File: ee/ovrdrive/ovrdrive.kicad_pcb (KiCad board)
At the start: 4 copper layers, 36.4 x 15 mm, 53 parts, among them J2 USB3_A, J4 Micro_SD_Card_Det_Hirose_DM3AT, SW1 SW_Push, U1 CH569W, U2 TLV62569DBV, U3 TLV62569DBV, Y2 30Mhz

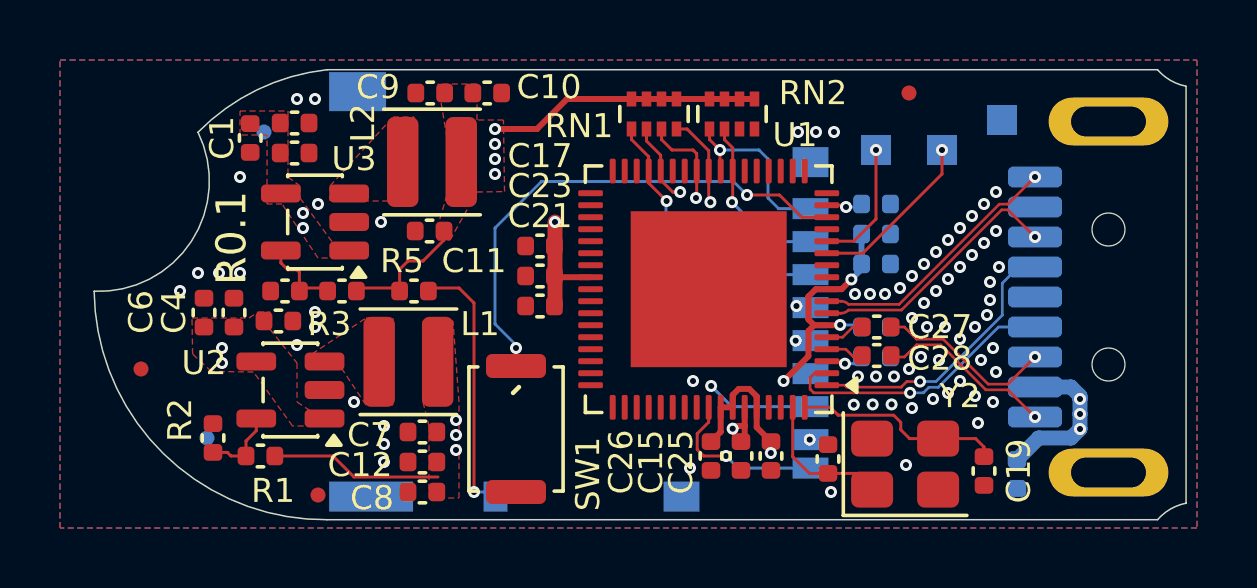
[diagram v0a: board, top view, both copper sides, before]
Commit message: Fixed SDIO pinout, length matched SDIO traces.
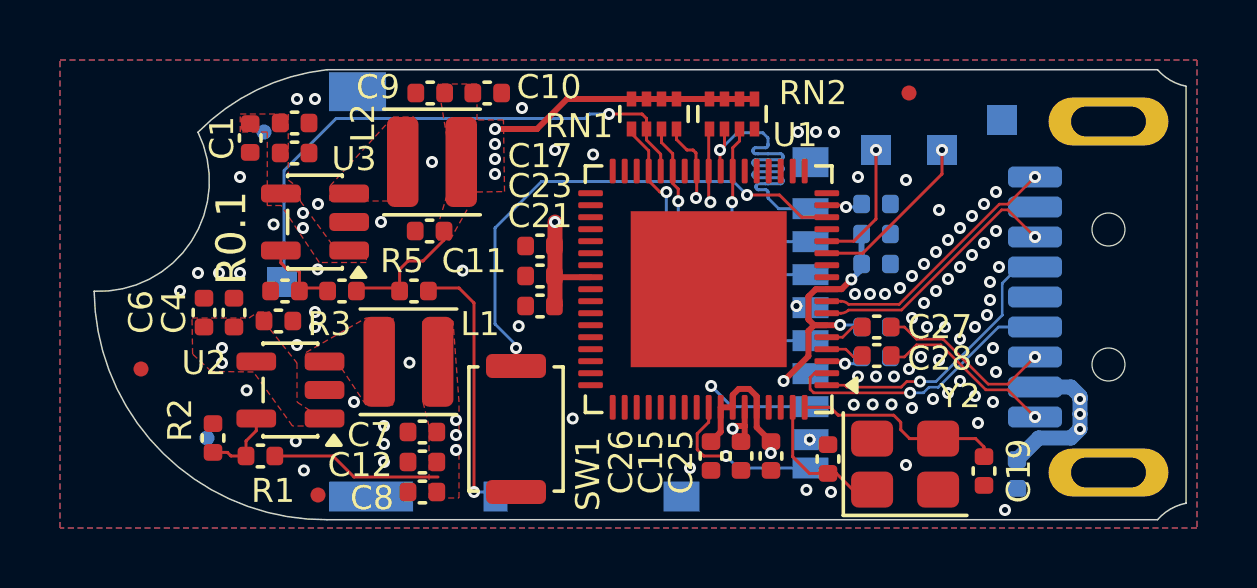
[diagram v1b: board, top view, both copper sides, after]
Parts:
- added TP4: TestPoint, TestPoint:TestPoint_Pad_1.0x1.0mm, B.Cu at (114.3, 103.7)
- C19, C20: value ? -> 15pF
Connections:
- RN1 pad 1: /SD_CMD -> /SD_CLK
- RN1 pad 2: /SD_CLK -> /RST#
- RN1 pad 3: /SD_D0 -> /SD_CMD
- RN1 pad 4: /SD_D1 -> /SD_D0
- RN2 pad 1: /SD_D2 -> /SD_D1
- RN2 pad 2: /SD_D3 -> /SD_D2
- RN2 pad 3: unconnected-(RN2-R3.1-Pad3) -> /SD_D3
- U1 pad 29: unconnected-(U1-PB16-Pad29) -> /SD_CMD
- U1 pad 30: /SD_CLK -> /RST#
- U1 pad 31: /SD_CMD -> /SD_CLK
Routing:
- net /RST#: track 0.00 -> 18.6 mm, vias 0 -> 1
- net /SD_D3: track 5.73 -> 12.7 mm
- net /SD_D2: track 6.12 -> 13.1 mm
- net /SD_CMD: track 9.78 -> 12.8 mm
- net /SD_CLK: track 11.2 -> 12.9 mm, vias 2 -> 1
- net /SD_D1: track 12.4 -> 13.2 mm
- net GND: vias 70 -> 87
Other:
- board text added: "90 Ohm Controlled Impedance"
